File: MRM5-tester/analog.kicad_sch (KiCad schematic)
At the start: 30 parts, among them IC2 OPA567AIRHGT, T1 ZMPT107-1, U2 ADA4661-2ACPZ-RL

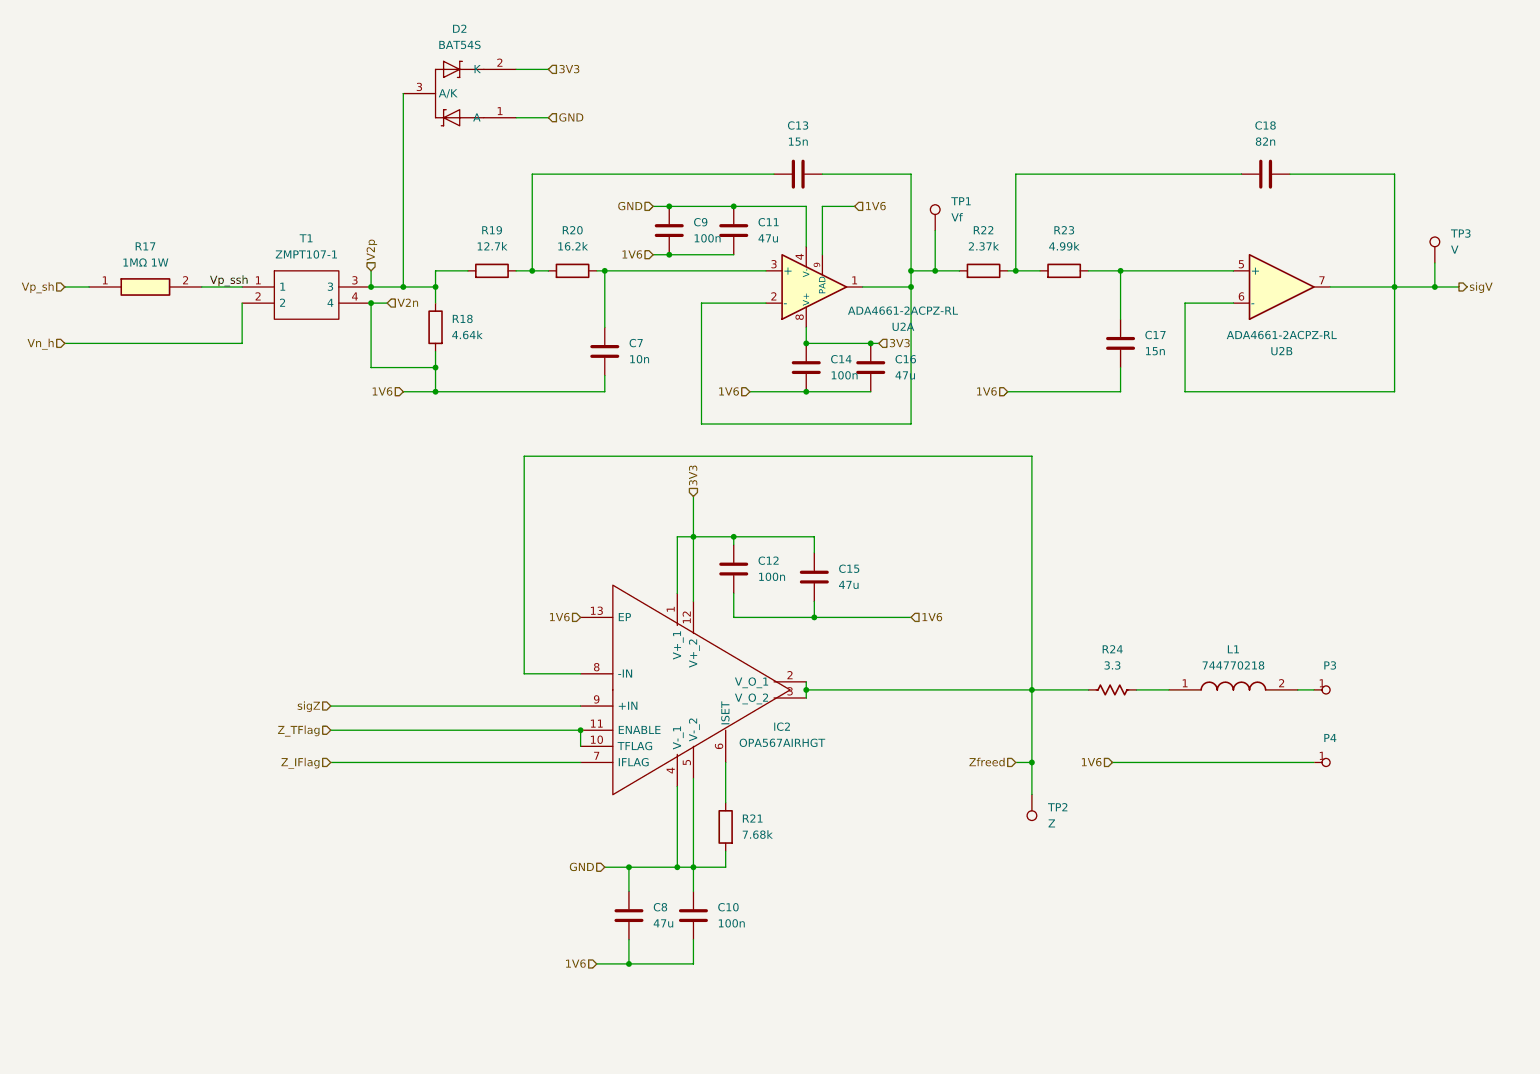
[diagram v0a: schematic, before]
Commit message: 전류 입력시의 경우를 고려한 회로 추가
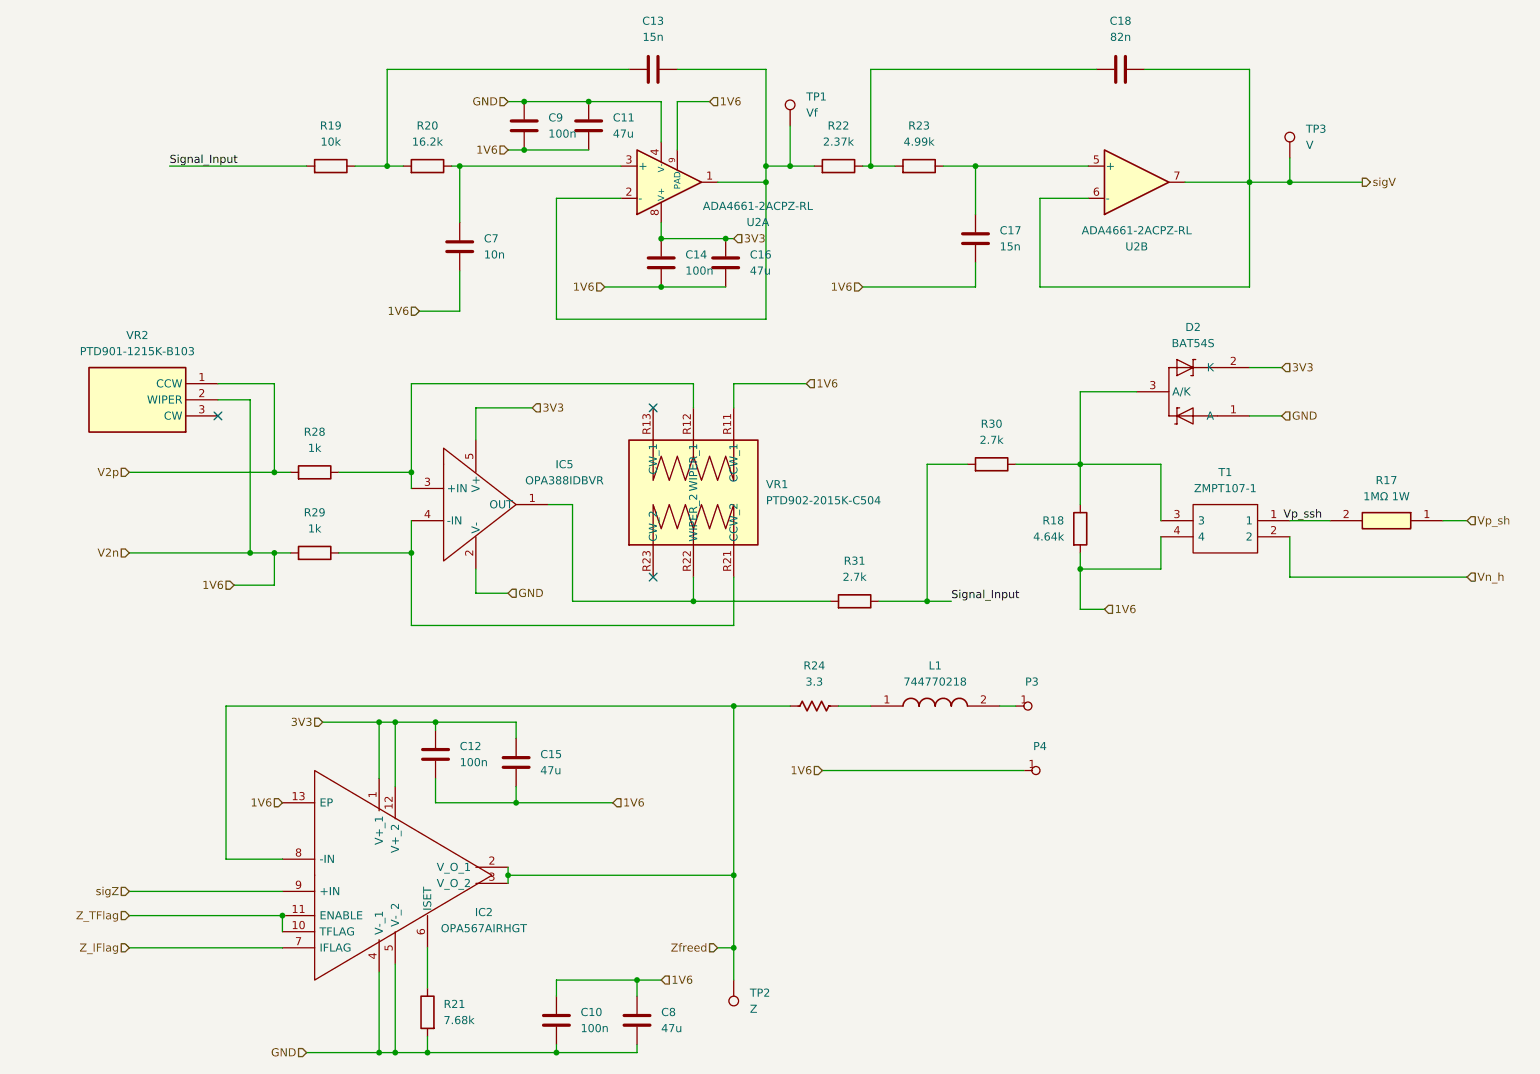
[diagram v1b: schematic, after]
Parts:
- added IC5: OPA388IDBVR, SOT95P280X145-5N, symbol Mouser:OPA388IDBVR
- added R28, R29: 1k, PCM_Resistor_SMD_AKL:R_0402_1005Metric, symbol PCM_Resistor_AKL:R_0402
- added R30, R31: 2.7k, PCM_Resistor_SMD_AKL:R_0402_1005Metric, symbol PCM_Resistor_AKL:R_0402
- added VR1: PTD902-2015K-C504, PTD9022015KC504, symbol Mouser:PTD902-2015K-C504
- added VR2: PTD901-1215K-B103, PTD9011015FA203, symbol Mouser:PTD901-1015F-A203
- R19: value 12.7k -> 10k
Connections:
- net 1V6: now also C8.1, R29.1, VR1.R11 (CCW_1), VR2.2 (WIPER); no longer C8.2
- net 3V3: now also IC5.5 (V+)
- net GND: now also C8.2, IC5.2 (V-); no longer C8.1
- net V2p: now also R28.1, VR2.1 (CCW); no longer D2.3 (A/K), R18.2, R19.1, T1.3
- new net: IC5.1 (OUT), R31.1, VR1.R22 (WIPER_2)
- new net: D2.3 (A/K), R18.2, R30.2, T1.3
- new net: IC5.3 (+IN), R28.2, VR1.R12 (WIPER_1)
- new net: IC5.4 (-IN), R29.2, VR1.R21 (CCW_2)
- new net Signal_Input: R19.1, R30.1, R31.2
- no-connect marks 0 -> 3
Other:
- moved on the sheet: C11, C13, C14, C16, C17, C18, C7, C9, R19, R20, R22, R23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

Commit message: 케이스에 마춰서 제작 중
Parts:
- IC5: footprint SOT95P280X145-5N -> Mouser:SOT95P280X145-5N
- VR1: footprint PTD9022015KC504 -> Mouser:PTD9022015KC504
- VR2: footprint PTD9011015FA203 -> Mouser:PTD9011015FA203
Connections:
- net 1V6: now also T1.3; no longer T1.4
- net Vn_h: now also R17.1; no longer T1.2
- net Vp_sh: now also T1.1; no longer R17.1
- net Vp_ssh: now also T1.2; no longer T1.1
- net PT1: now reaches D2.3 (A/K), R18.2, R30.2
- net PT1: now also T1.4; no longer T1.3
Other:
- moved on the sheet: P4

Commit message: 1차 마감
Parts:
- U2: value ADA4661-2ACPZ-RL -> ADA4500-2ACPZ
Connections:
- net 1V6: no longer T1.3
- net PT1: no longer T1.4
- new net PT1_bot: T1.4
- new net PT2_bot: T1.3
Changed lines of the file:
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@@
 		)
 	)
-	(hierarchical_label "PT2"
+	(hierarchical_label "PT2_bot"
 		(shape input)
 		(at 203.2 140.97 180)
@@
 		)
 	)
-	(hierarchical_label "PT1"
+	(hierarchical_label "PT1_bot"
 		(shape input)
 		(at 203.2 143.51 180)
@@
 			)
 		)
-		(property "Value" "ADA4661-2ACPZ-RL"
+		(property "Value" "ADA4500-2ACPZ"
 			(at 147.32 52.0386 0)
 			(effects
@@
 			)
 		)
-		(property "Value" "ADA4661-2ACPZ-RL"
+		(property "Value" "ADA4500-2ACPZ"
 			(at 207.01 55.88 0)
 			(effects

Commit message: updated
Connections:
- net 1V6: no longer IC2.13 (EP)
- net Vn_h renamed Vn_sh
- no-connect marks 3 -> 4
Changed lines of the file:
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@@
+	)
+	(no_connect
+		(at 72.39 146.05)
 	)
 	(no_connect
@@
 		)
 	)
-	(hierarchical_label "Vn_h"
+	(hierarchical_label "Vn_sh"
 		(shape input)
 		(at 260.35 143.51 0)
@@
 		(fields_autoplaced yes)
 		(effects
-			(font
-				(size 1.27 1.27)
-			)
-			(justify right)
-		)
-	)
-	(hierarchical_label "1V6"
-		(shape input)
-		(at 72.39 146.05 180)
-		(fields_autoplaced yes)
-		(effects

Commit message: firmware updated
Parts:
- renumbered C9 to C10, C10 to C11, C11 to C12, C8 to C13, C13 to C14, C14 to C15, C12 to C7, C7 to C8, C15 to C9, IC5 to IC3, R28 to R17, R29 to R18, R24 to R22, R22 to R23, R31 to R24, R23 to R25, R30 to R26, R18 to R27, R17 to R28, TP2 to TP1, TP1 to TP2, VR2 to VR1, VR1 to VR2
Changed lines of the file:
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@@
 		(dnp no)
 		(fields_autoplaced yes)
-		(property "Reference" "VR2"
+		(property "Reference" "VR1"
 			(at 49.53 72.39 0)
 			(effects
@@
 			(project ""
 				(path "/6e775c75-0b09-4e5f-9bff-c5585ac94ad7/d46285ed-39e7-481d-bc83-4a7d1879f6d2"
-					(reference "VR2")
+					(reference "VR1")
 					(unit 1)
 				)
@@
 		(dnp no)
 		(fields_autoplaced yes)
-		(property "Reference" "C8"
+		(property "Reference" "C13"
 			(at 132.08 179.0699 0)
 			(effects
@@
 			(project "MRM5-tester"
 				(path "/6e775c75-0b09-4e5f-9bff-c5585ac94ad7/d46285ed-39e7-481d-bc83-4a7d1879f6d2"
-					(reference "C8")
+					(reference "C13")
 					(unit 1)
 				)
@@
 		(dnp no)
 		(fields_autoplaced yes)
-		(property "Reference" "R23"
+		(property "Reference" "R25"
 			(at 172.72 39.37 90)
 			(effects
@@
 			(project "MRM5-tester"
 				(path "/6e775c75-0b09-4e5f-9bff-c5585ac94ad7/d46285ed-39e7-481d-bc83-4a7d1879f6d2"
-					(reference "R23")
+					(reference "R25")
 					(unit 1)
 				)
@@
 		(dnp no)
 		(fields_autoplaced yes)
-		(property "Reference" "R31"
+		(property "Reference" "R24"
 			(at 162.56 107.95 90)
 			(effects
@@
 			(project "MRM5-tester"
 				(path "/6e775c75-0b09-4e5f-9bff-c5585ac94ad7/d46285ed-39e7-481d-bc83-4a7d1879f6d2"
-					(reference "R31")
+					(reference "R24")
 					(unit 1)
 				)
@@
 		(dnp no)
 		(fields_autoplaced yes)
-		(property "Reference" "C12"
+		(property "Reference" "C7"
 			(at 100.33 137.1599 0)
 			(effects
@@
 			(project "MRM5-tester"
 				(path "/6e775c75-0b09-4e5f-9bff-c5585ac94ad7/d46285ed-39e7-481d-bc83-4a7d1879f6d2"
-					(reference "C12")
+					(reference "C7")
 					(unit 1)
 				)
@@
 		(dnp no)
 		(fields_autoplaced yes)
-		(property "Reference" "TP2"
+		(property "Reference" "TP1"
 			(at 146.05 176.0219 0)
 			(effects
@@
 			(project "MRM5-tester"
 				(path "/6e775c75-0b09-4e5f-9bff-c5585ac94ad7/d46285ed-39e7-481d-bc83-4a7d1879f6d2"
-					(reference "TP2")
+					(reference "TP1")
 					(unit 1)
 				)
@@
 		(dnp no)
 		(fields_autoplaced yes)
-		(property "Reference" "C9"
+		(property "Reference" "C10"
 			(at 114.3 38.0999 0)
 			(effects
@@
 			(project "MRM5-tester"
 				(path "/6e775c75-0b09-4e5f-9bff-c5585ac94ad7/d46285ed-39e7-481d-bc83-4a7d1879f6d2"
-					(reference "C9")
+					(reference "C10")
 					(unit 1)
 				)
@@
 		(dnp no)
 		(fields_autoplaced yes)
-		(property "Reference" "C11"
+		(property "Reference" "C12"
 			(at 124.46 38.0999 0)
 			(effects
@@
 			(project "MRM5-tester"
 				(path "/6e775c75-0b09-4e5f-9bff-c5585ac94ad7/d46285ed-39e7-481d-bc83-4a7d1879f6d2"
-					(reference "C11")
+					(reference "C12")
 					(unit 1)
 				)
@@
 		(dnp no)
 		(fields_autoplaced yes)
-		(property "Reference" "R22"
+		(property "Reference" "R23"
 			(at 160.02 39.37 90)
 			(effects
@@
 			(project "MRM5-tester"
 				(path "/6e775c75-0b09-4e5f-9bff-c5585ac94ad7/d46285ed-39e7-481d-bc83-4a7d1879f6d2"
-					(reference "R22")
+					(reference "R23")
 					(unit 1)
 				)
@@
 		(dnp no)
 		(fields_autoplaced yes)
-		(property "Reference" "R24"
+		(property "Reference" "R22"
 			(at 156.21 124.46 90)
 			(effects
@@
 			(project "MRM5-tester"
 				(path "/6e775c75-0b09-4e5f-9bff-c5585ac94ad7/d46285ed-39e7-481d-bc83-4a7d1879f6d2"
-					(reference "R24")
+					(reference "R22")
 					(unit 1)
 				)
@@
 		(dnp no)
 		(fields_autoplaced yes)
-		(property "Reference" "VR1"
+		(property "Reference" "VR2"
 			(at 148.59 95.8849 90)
 			(effects
@@
 			(project ""
 				(path "/6e775c75-0b09-4e5f-9bff-c5585ac94ad7/d46285ed-39e7-481d-bc83-4a7d1879f6d2"
-					(reference "VR1")
+					(reference "VR2")
 					(unit 1)
 				)
@@
 		(dnp no)
 		(fields_autoplaced yes)
-		(property "Reference" "C7"
+		(property "Reference" "C8"
 			(at 104.14 57.1499 0)
 			(effects
@@
 			(project "MRM5-tester"
 				(path "/6e775c75-0b09-4e5f-9bff-c5585ac94ad7/d46285ed-39e7-481d-bc83-4a7d1879f6d2"
-					(reference "C7")
+					(reference "C8")
 					(unit 1)
 				)
@@
 		(dnp no)
 		(fields_autoplaced yes)
-		(property "Reference" "R17"
+		(property "Reference" "R28"
 			(at 247.65 137.16 0)
 			(effects
@@
 			(project "MRM5-tester"
 				(path "/6e775c75-0b09-4e5f-9bff-c5585ac94ad7/d46285ed-39e7-481d-bc83-4a7d1879f6d2"
-					(reference "R17")
+					(reference "R28")
 					(unit 1)
 				)
@@
 		(dnp no)
 		(fields_autoplaced yes)
-		(property "Reference" "C13"
+		(property "Reference" "C14"
 			(at 130.81 22.86 90)
 			(effects
@@
 			(project "MRM5-tester"
 				(path "/6e775c75-0b09-4e5f-9bff-c5585ac94ad7/d46285ed-39e7-481d-bc83-4a7d1879f6d2"
-					(reference "C13")
+					(reference "C14")
 					(unit 1)
 				)
@@
 		(dnp no)
 		(fields_autoplaced yes)
-		(property "Reference" "R28"
+		(property "Reference" "R17"
 			(at 77.47 87.63 90)
 			(effects
@@
 			(project "MRM5-tester"
 				(path "/6e775c75-0b09-4e5f-9bff-c5585ac94ad7/d46285ed-39e7-481d-bc83-4a7d1879f6d2"
-					(reference "R28")
+					(reference "R17")
 					(unit 1)
 				)
@@
 		(dnp no)
 		(fields_autoplaced yes)
-		(property "Reference" "C15"
+		(property "Reference" "C9"
 			(at 113.03 138.4299 0)
 			(effects
@@
 			(project "MRM5-tester"
 				(path "/6e775c75-0b09-4e5f-9bff-c5585ac94ad7/d46285ed-39e7-481d-bc83-4a7d1879f6d2"
-					(reference "C15")
+					(reference "C9")
 					(unit 1)
 				)
@@
 		(dnp no)
 		(fields_autoplaced yes)
-		(property "Reference" "C10"
+		(property "Reference" "C11"
 			(at 119.38 179.0699 0)
 			(effects
@@
 			(project "MRM5-tester"
 				(path "/6e775c75-0b09-4e5f-9bff-c5585ac94ad7/d46285ed-39e7-481d-bc83-4a7d1879f6d2"
-					(reference "C10")
+					(reference "C11")
 					(unit 1)
 				)
@@
 		(dnp no)
 		(fields_autoplaced yes)
-		(property "Reference" "R29"
+		(property "Reference" "R18"
 			(at 77.47 100.33 90)
 			(effects
@@
 			(project "MRM5-tester"
 				(path "/6e775c75-0b09-4e5f-9bff-c5585ac94ad7/d46285ed-39e7-481d-bc83-4a7d1879f6d2"
-					(reference "R29")
+					(reference "R18")
 					(unit 1)
 				)
@@
 		(dnp no)
 		(fields_autoplaced yes)
-		(property "Reference" "TP1"
+		(property "Reference" "TP2"
 			(at 154.94 34.7979 0)
 			(effects
@@
 			(project "MRM5-tester"
 				(path "/6e775c75-0b09-4e5f-9bff-c5585ac94ad7/d46285ed-39e7-481d-bc83-4a7d1879f6d2"
-					(reference "TP1")
+					(reference "TP2")
 					(unit 1)
 				)
@@
 		(dnp no)
 		(fields_autoplaced yes)
-		(property "Reference" "R18"
+		(property "Reference" "R27"
 			(at 195.58 101.5999 0)
 			(effects
@@
 			(project "MRM5-tester"
 				(path "/6e775c75-0b09-4e5f-9bff-c5585ac94ad7/d46285ed-39e7-481d-bc83-4a7d1879f6d2"
-					(reference "R18")
+					(reference "R27")
 					(unit 1)
 				)
@@
 		(dnp no)
 		(fields_autoplaced yes)
-		(property "Reference" "R30"
+		(property "Reference" "R26"
 			(at 184.15 86.36 90)
 			(effects
@@
 			(project "MRM5-tester"
 				(path "/6e775c75-0b09-4e5f-9bff-c5585ac94ad7/d46285ed-39e7-481d-bc83-4a7d1879f6d2"
-					(reference "R30")
+					(reference "R26")
 					(unit 1)
 				)
@@
 		(dnp no)
 		(fields_autoplaced yes)
-		(property "Reference" "C14"
+		(property "Reference" "C15"
 			(at 135.89 59.6899 0)
 			(effects
@@
 			(project "MRM5-tester"
 				(path "/6e775c75-0b09-4e5f-9bff-c5585ac94ad7/d46285ed-39e7-481d-bc83-4a7d1879f6d2"
-					(reference "C14")
+					(reference "C15")
 					(unit 1)
 				)
@@
 		(dnp no)
 		(fields_autoplaced yes)
-		(property "Reference" "IC5"
+		(property "Reference" "IC3"
 			(at 116.84 92.7414 0)
 			(effects
@@
 			(project ""
 				(path "/6e775c75-0b09-4e5f-9bff-c5585ac94ad7/d46285ed-39e7-481d-bc83-4a7d1879f6d2"
-					(reference "IC5")
+					(reference "IC3")
 					(unit 1)
 				)

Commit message: tester updated
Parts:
- R22: value 3.3 -> 22
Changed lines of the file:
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@@
 	(label "Vp_ssh"
 		(at 237.49 143.51 180)
-		(fields_autoplaced yes)
 		(effects
 			(font
@@
 	(label "Signal_Input"
 		(at 54.61 45.72 0)
-		(fields_autoplaced yes)
 		(effects
 			(font
@@
 	(label "Signal_Input"
 		(at 177.8 114.3 0)
-		(fields_autoplaced yes)
 		(effects
 			(font
@@
 		(shape input)
 		(at 111.76 83.82 0)
-		(fields_autoplaced yes)
 		(effects
 			(font
@@
 		(shape input)
 		(at 229.87 109.22 0)
-		(fields_autoplaced yes)
 		(effects
 			(font
@@
 		(shape input)
 		(at 156.21 156.21 180)
-		(fields_autoplaced yes)
 		(effects
 			(font
@@
 		(shape input)
 		(at 78.74 133.35 180)
-		(fields_autoplaced yes)
 		(effects
 			(font
@@
 		(shape input)
 		(at 260.35 132.08 0)
-		(fields_autoplaced yes)
 		(effects
 			(font
@@
 		(shape input)
 		(at 93.98 68.58 180)
-		(fields_autoplaced yes)
 		(effects
 			(font
@@
 		(shape input)
 		(at 203.2 140.97 180)
-		(fields_autoplaced yes)
 		(effects
 			(font
@@
 		(shape input)
 		(at 64.77 111.76 180)
-		(fields_autoplaced yes)
 		(effects
 			(font
@@
 		(shape input)
 		(at 124.46 146.05 0)
-		(fields_autoplaced yes)
 		(effects
 			(font
@@
 		(shape input)
 		(at 48.26 163.83 180)
-		(fields_autoplaced yes)
 		(effects
 			(font
@@
 		(shape input)
 		(at 132.08 173.99 0)
-		(fields_autoplaced yes)
 		(effects
 			(font
@@
 		(shape input)
 		(at 48.26 168.91 180)
-		(fields_autoplaced yes)
 		(effects
 			(font
@@
 		(shape input)
 		(at 123.19 64.77 180)
-		(fields_autoplaced yes)
 		(effects
 			(font
@@
 		(shape input)
 		(at 201.93 115.57 0)
-		(fields_autoplaced yes)
 		(effects
 			(font
@@
 		(shape input)
 		(at 139.7 35.56 0)
-		(fields_autoplaced yes)
 		(effects
 			(font
@@
 		(shape input)
 		(at 76.2 185.42 180)
-		(fields_autoplaced yes)
 		(effects
 			(font
@@
 		(shape input)
 		(at 107.95 35.56 180)
-		(fields_autoplaced yes)
 		(effects
 			(font
@@
 		(shape input)
 		(at 163.83 64.77 180)
-		(fields_autoplaced yes)
 		(effects
 			(font
@@
 		(shape input)
 		(at 48.26 106.68 180)
-		(fields_autoplaced yes)
 		(effects
 			(font
@@
 		(shape input)
 		(at 229.87 92.71 0)
-		(fields_autoplaced yes)
 		(effects
 			(font
@@
 		(shape input)
 		(at 260.35 143.51 0)
-		(fields_autoplaced yes)
 		(effects
 			(font
@@
 		(shape input)
 		(at 140.97 168.91 180)
-		(fields_autoplaced yes)
 		(effects
 			(font
@@
 		(shape input)
 		(at 229.87 85.09 0)
-		(fields_autoplaced yes)
 		(effects
 			(font
@@
 		(shape input)
 		(at 203.2 143.51 180)
-		(fields_autoplaced yes)
 		(effects
 			(font
@@
 		(shape output)
 		(at 242.57 48.26 0)
-		(fields_autoplaced yes)
 		(effects
 			(font
@@
 		(shape input)
 		(at 229.87 77.47 0)
-		(fields_autoplaced yes)
 		(effects
 			(font
@@
 		(shape input)
 		(at 154.94 80.01 0)
-		(fields_autoplaced yes)
 		(effects
 			(font
@@
 		(shape input)
 		(at 48.26 160.02 180)
-		(fields_autoplaced yes)
 		(effects
 			(font
@@
 		(shape input)
 		(at 107.95 43.18 180)
-		(fields_autoplaced yes)
 		(effects
 			(font
@@
 		(shape input)
 		(at 48.26 93.98 180)
-		(fields_autoplaced yes)
 		(effects
 			(font
@@
 		(shape input)
 		(at 107.95 113.03 0)
-		(fields_autoplaced yes)
 		(effects
 			(font
@@
 		(shape input)
 		(at 143.51 57.15 0)
-		(fields_autoplaced yes)
 		(effects
 			(font
@@
 			)
 		)
-		(property "Value" "3.3"
+		(property "Value" "22"
 			(at 156.21 127 90)
 			(effects
